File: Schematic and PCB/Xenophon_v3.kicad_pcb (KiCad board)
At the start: 2 copper layers, 301.5 x 121 mm, 190 parts, among them J1 USB_C_Receptacle_USB2.0, J2 AudioJack3, J3 USB_C_Receptacle_USB2.0, J4 AudioJack3, SW1 SW_Push, SW10 SW_Push, SW11 SW_Push, SW12 SW_Push, SW13 SW_Push, SW14 SW_Push, SW15 SW_Push, SW16 SW_Push, SW17 SW_Push, SW18 SW_Push, SW19 SW_Push, SW2 SW_Push, SW20 SW_Push, SW21 SW_Push, SW22 SW_Push, SW23 SW_Push, SW24 SW_Push, SW25 SW_Push, SW26 SW_Push, SW27 SW_Push, SW28 SW_Push, SW29 SW_Push, SW3 SW_Push, SW30 SW_Push, SW31 SW_Push, SW32 SW_Push, SW33 SW_Push, SW34 SW_Push, SW35 SW_Push, SW36 SW_Push, SW37 SW_Push, SW38 SW_Push, SW39 SW_Push, SW4 SW_Push, SW40 SW_Push, SW41 SW_Push, SW42 SW_Push, SW43 SW_Push, SW44 SW_Push, SW45 SW_Push, SW46 SW_Push, SW47 SW_Push, SW48 SW_Push, SW49 SW_Push, SW5 SW_Push, SW50 SW_Push, SW51 SW_Push, SW52 SW_Push, SW53 SW_Push, SW54 SW_Push, SW55 SW_Push, SW56 SW_Push, SW57 SW_Push, SW58 SW_Push, SW59 SW_Push, SW6 SW_Push, SW60 SW_Push, SW61 SW_Push, SW62 SW_Push, SW63 SW_Push, SW64 SW_Push, SW65 SW_Push, SW66 SW_Push, SW67 SW_Push, SW68 SW_Push, SW69 SW_Push, SW7 SW_Push, SW70 SW_Push, SW8 SW_Push, SW9 SW_Push, U1 ATmega32U4-A, U2 ATmega32U4-A, Y1 Crystal, Y2 Crystal

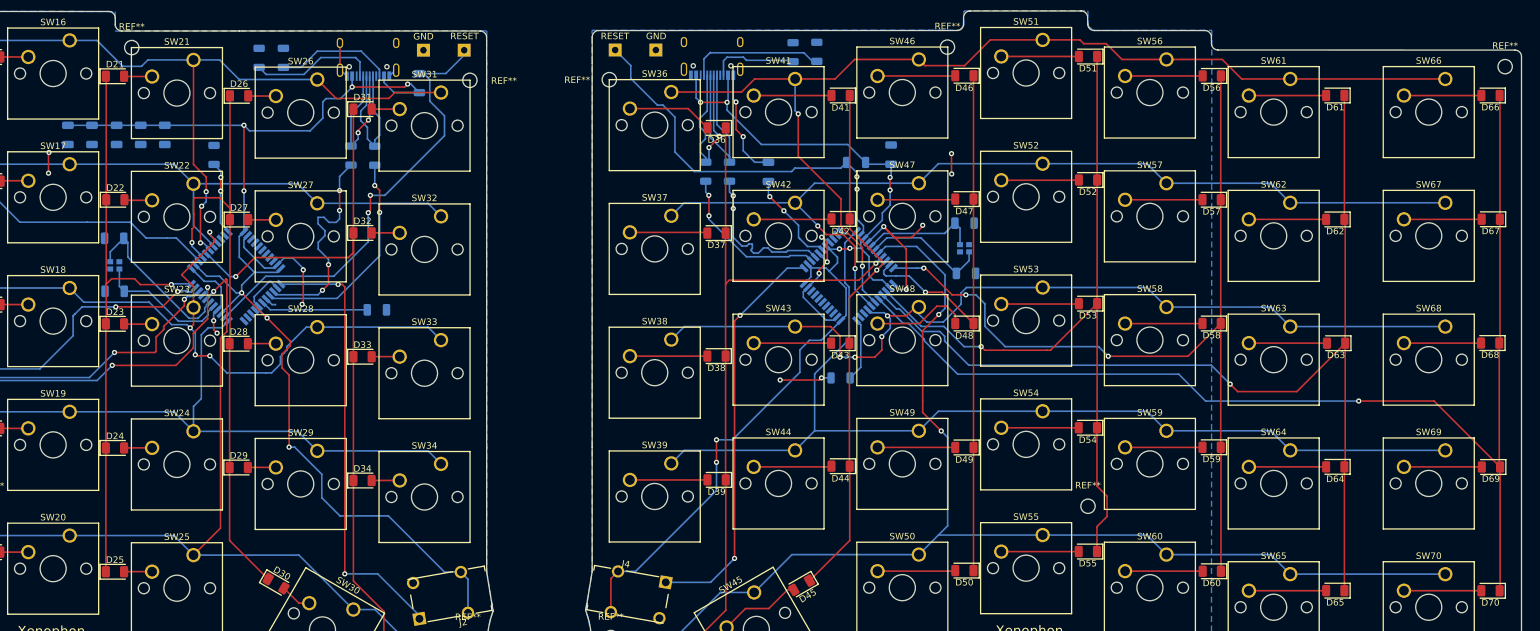
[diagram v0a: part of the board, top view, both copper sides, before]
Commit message: Small rerouting fixes
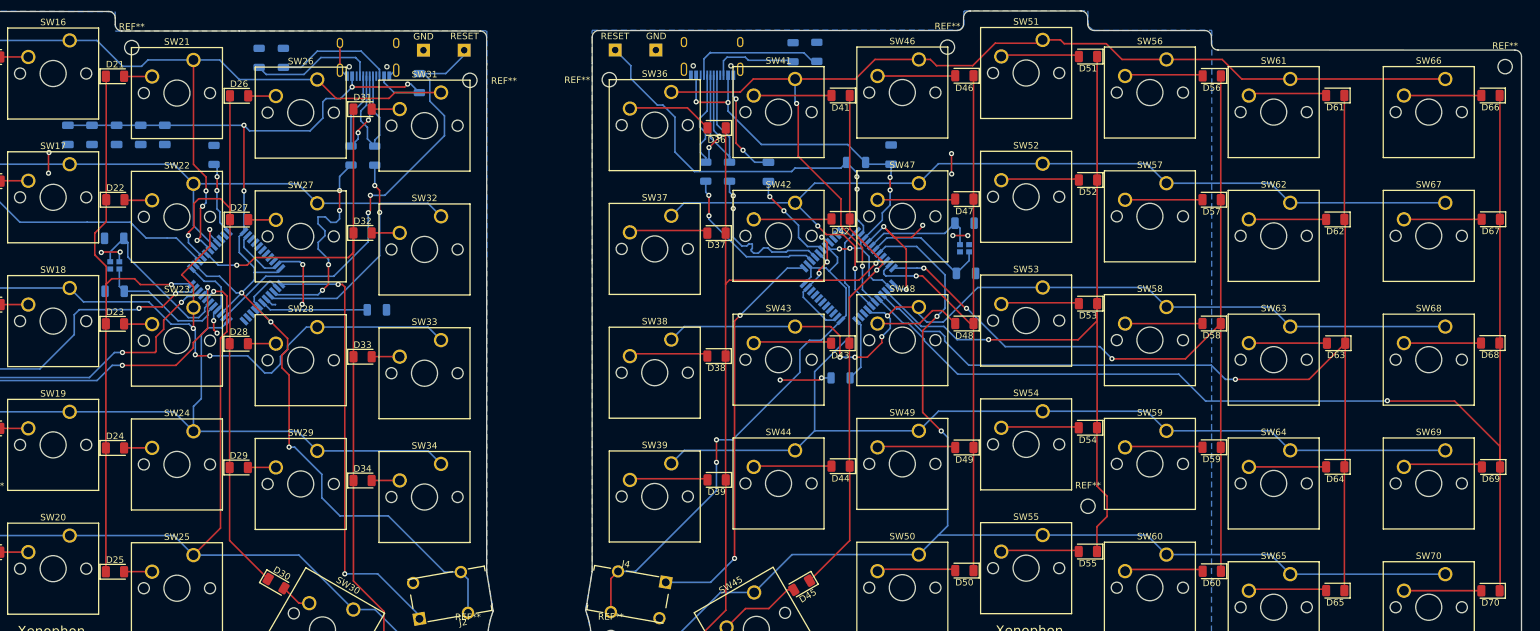
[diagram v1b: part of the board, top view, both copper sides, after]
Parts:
- added REF**: KiCad-Logo2_5mm_SilkScreen, Symbol:KiCad-Logo2_5mm_SilkScreen, B.Cu at (269.5, 134.2)
- added REF**: OSHW-Logo2_7.3x6mm_SilkScreen, Symbol:OSHW-Logo2_7.3x6mm_SilkScreen, B.Cu at (27.2, 134.8)
- added REF**: OSHW-Logo2_7.3x6mm_SilkScreen, Symbol:OSHW-Logo2_7.3x6mm_SilkScreen, B.Cu at (257.7, 134.7)
- added REF**: KiCad-Logo2_5mm_SilkScreen, Symbol:KiCad-Logo2_5mm_SilkScreen, B.Cu at (39.0, 134.3)
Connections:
- Y1 pad 3: (no net) -> GND
- Y1 pad 4: (no net) -> GND
- Y2 pad 3: (no net) -> RGND
- Y2 pad 4: (no net) -> RGND
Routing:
- net GND: track 45.0 -> 49.3 mm, vias 6 -> 8
- net /ButtonSheet/row5: track 184.9 -> 181.9 mm
- net RGND: track 73.7 -> 76.0 mm, vias 12 -> 14
- net /RightButtonSheet/column7: track 182.4 -> 184.5 mm
- net /RightButtonSheet/column5: track 136.0 -> 134.3 mm
- net /RightButtonSheet/row3: track 140.3 -> 138.7 mm
- net /RightButtonSheet/column6: track 156.8 -> 155.2 mm
- net /ButtonSheet/column7: track 114.3 -> 112.8 mm
- net /ButtonSheet/column5: track 90.0 -> 91.5 mm
- net Net-(D48-Pad2): track 14.9 -> 13.6 mm
- net /ButtonSheet/row1: track 157.3 -> 157.8 mm
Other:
- board text added: "@lillkakan"

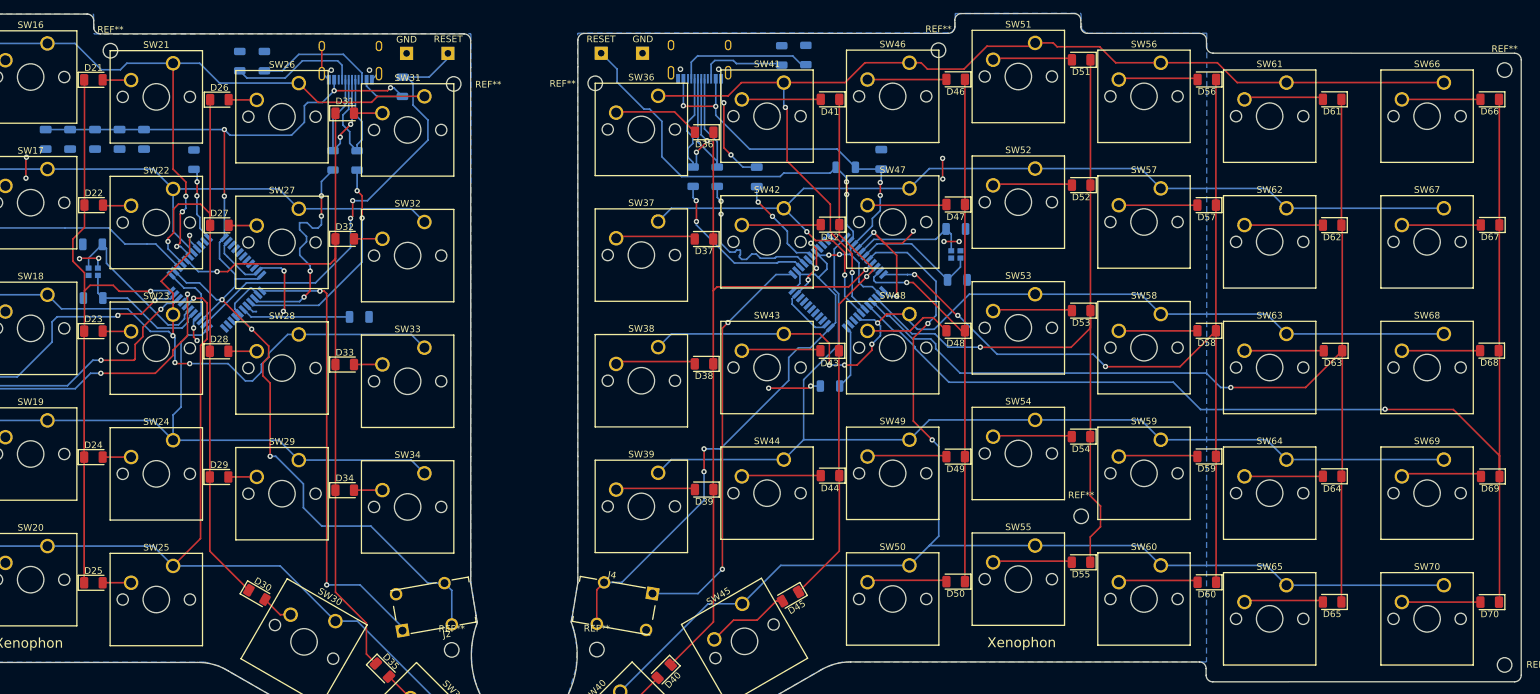
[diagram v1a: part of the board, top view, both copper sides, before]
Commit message: Panelized the pcb
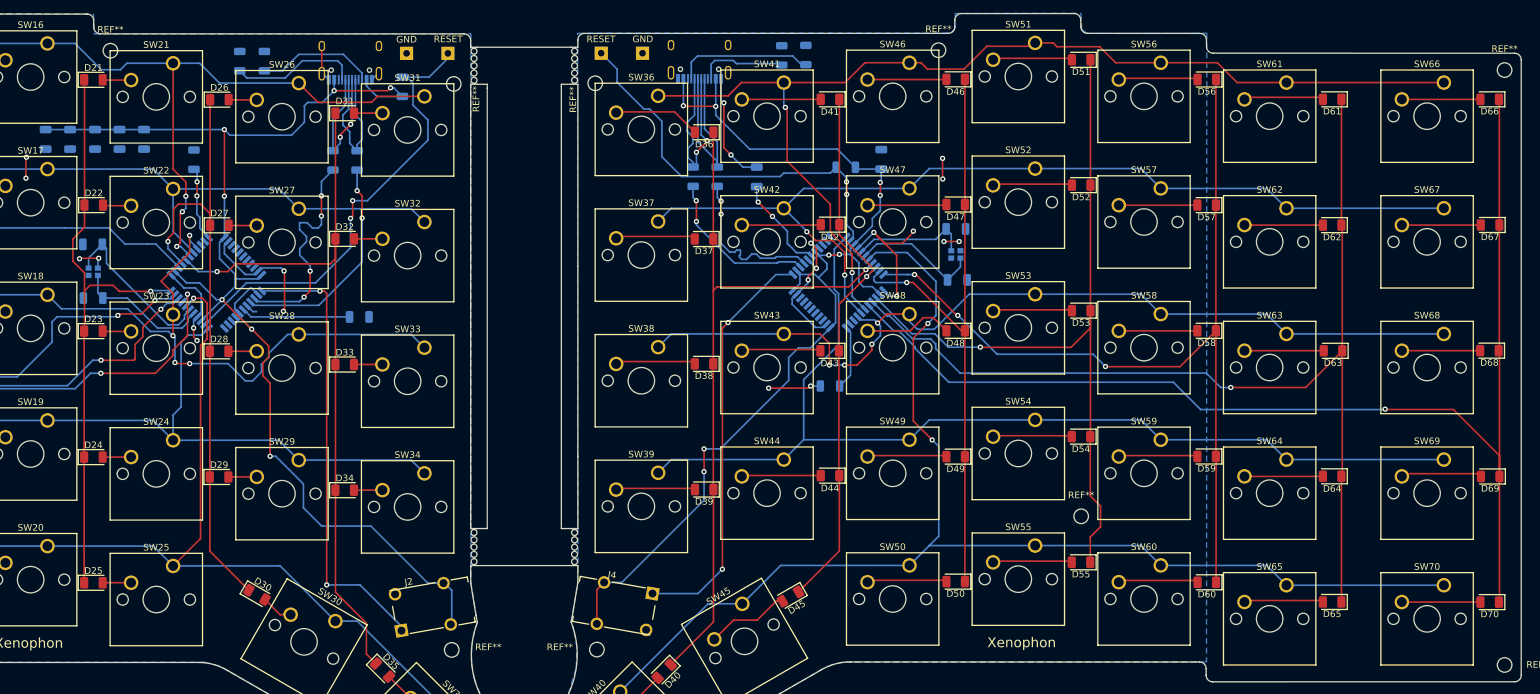
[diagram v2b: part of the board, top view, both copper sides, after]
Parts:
- moved J2 0.15 mm to (137.2, 126.9)
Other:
- outline, holes or cut-outs redrawn
- board text added: "MountingHole_2.2mm_M2"

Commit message: Updated readme and qmk code
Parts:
- moved R3 1.04 mm to (111.0, 43.7)
- moved R4 1.04 mm to (107.3, 43.7)
